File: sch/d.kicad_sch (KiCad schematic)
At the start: 1 part

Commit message: Update
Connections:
- net GND: now reaches J?.14 (-12V)
- net GND: now also J?.15 (GND), J?.17 (GND), J?.18 (GND), J?.19 (GND), J?.24 (GND), J?.3 (GND), J?.5 (GND), J?.7 (GND)
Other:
- moved on the sheet: J?
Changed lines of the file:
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@@
 (kicad_sch (version 20211123) (generator eeschema)
   (paper "A4")
-  (symbol (lib_id "Connector:ATX-24") (at 152.4 95.25 0) (unit 1)
+  (junction (at 156.21 111.76) (diameter 0) (color 0 0 0 0)
+  )
+  (wire (pts (xy 172.72 111.76) (xy 172.72 105.41))
+    (stroke (width 0) (type default) (color 0 0 0 0))
+  )
+  (wire (pts (xy 156.21 111.76) (xy 156.21 113.03))
+    (stroke (width 0) (type default) (color 0 0 0 0))
+  )
+  (wire (pts (xy 172.72 105.41) (xy 168.91 105.41))
+    (stroke (width 0) (type default) (color 0 0 0 0))
+  )
+  (wire (pts (xy 156.21 111.76) (xy 172.72 111.76))
+    (stroke (width 0) (type default) (color 0 0 0 0))
+  )
+  (wire (pts (xy 156.21 110.49) (xy 156.21 111.76))
+    (stroke (width 0) (type default) (color 0 0 0 0))
+  )
+  (symbol (lib_id "power:GND") (at 156.21 113.03 0) (unit 1)
     (in_bom yes) (on_board yes) (fields_autoplaced)
-    (property "Reference" "J?" (id 0) (at 152.4 77.47 0))
-    (property "Value" "ATX-24" (id 1) (at 152.4 80.01 0))
-    (property "Footprint" "" (id 2) (at 152.4 97.79 0)
+    (property "Reference" "#PWR?" (id 0) (at 156.21 119.38 0)
       (effects (font (size 1.27 1.27)) hide)
     )
-    (property "Datasheet" "https://www.intel.com/content/dam/www/public/us/en/documents/guides/power-supply-design-guide-june.pdf#page=33" (id 3) (at 213.36 109.22 0)
+    (property "Value" "GND" (id 1) (at 156.21 118.11 0))
+    (property "Footprint" "" (id 2) (at 156.21 113.03 0)
       (effects (font (size 1.27 1.27)) hide)
     )
+    (property "Datasheet" "" (id 3) (at 156.21 113.03 0)
+      (effects (font (size 1.27 1.27)) hide)
+    )
+    (pin "1")
+  )
+  (symbol (lib_id "Connector:ATX-24") (at 156.21 95.25 0) (unit 1)
+    (in_bom yes) (on_board yes) (fields_autoplaced)
+    (property "Reference" "J?" (id 0) (at 156.21 77.47 0))
+    (property "Value" "ATX-24" (id 1) (at 156.21 80.01 0))
+    (property "Footprint" "" (id 2) (at 156.21 97.79 0)
+      (effects (font (size 1.27 1.27)) hide)
+    )
+    (property "Datasheet" "https://www.intel.com/content/dam/www/public/us/en/documents/guides/power-supply-design-guide-june.pdf#page=33" (id 3) (at 217.17 109.22 0)
+      (effects (font (size 1.27 1.27)) hide)
+    )

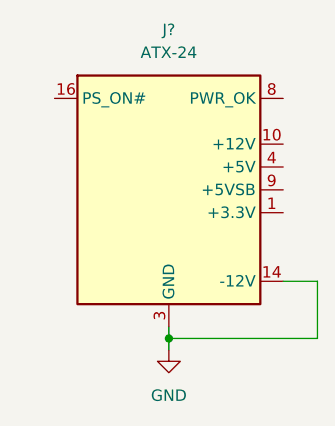
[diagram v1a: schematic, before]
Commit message: Add file and sheet instance with spaces. Anotate parts.
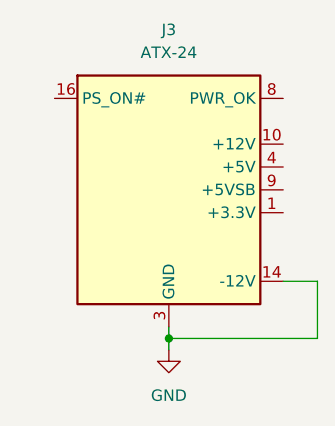
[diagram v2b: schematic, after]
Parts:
- gave numbers to parts that had none: 1
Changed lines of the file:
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@@
   (symbol (lib_id "power:GND") (at 156.21 113.03 0) (unit 1)
     (in_bom yes) (on_board yes) (fields_autoplaced)
-    (property "Reference" "#PWR?" (id 0) (at 156.21 119.38 0)
+    (property "Reference" "#PWR01" (id 0) (at 156.21 119.38 0)
       (effects (font (size 1.27 1.27)) hide)
     )
@@
   (symbol (lib_id "Connector:ATX-24") (at 156.21 95.25 0) (unit 1)
     (in_bom yes) (on_board yes) (fields_autoplaced)
-    (property "Reference" "J?" (id 0) (at 156.21 77.47 0))
+    (property "Reference" "J3" (id 0) (at 156.21 77.47 0))
     (property "Value" "ATX-24" (id 1) (at 156.21 80.01 0))
     (property "Footprint" "" (id 2) (at 156.21 97.79 0)
